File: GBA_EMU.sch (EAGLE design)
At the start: 72 parts, among them J1 USB-MINIB-5PIN, J2 AVR_SPI, Q1 MOSFET-PCHANNEL, SW1 LEFT, SW2 RIGHT, SW3 PWR_SWITCH, U2 FT230X, U4 LM4875, U5 V_REG_LDOSMD2, U7 AZV321, X2 HEADPHONE

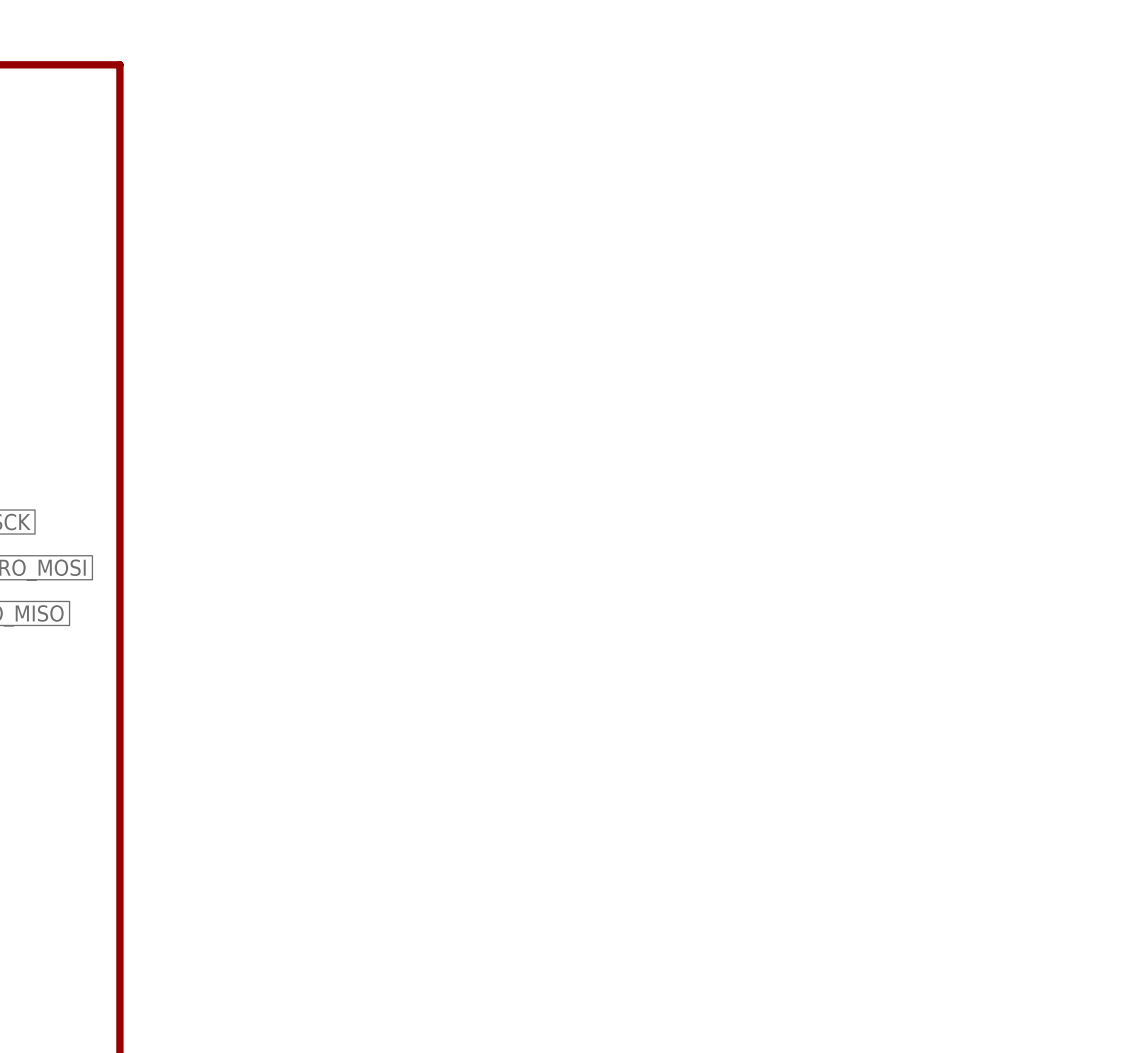
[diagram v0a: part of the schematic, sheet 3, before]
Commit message: added usb hub chip :)
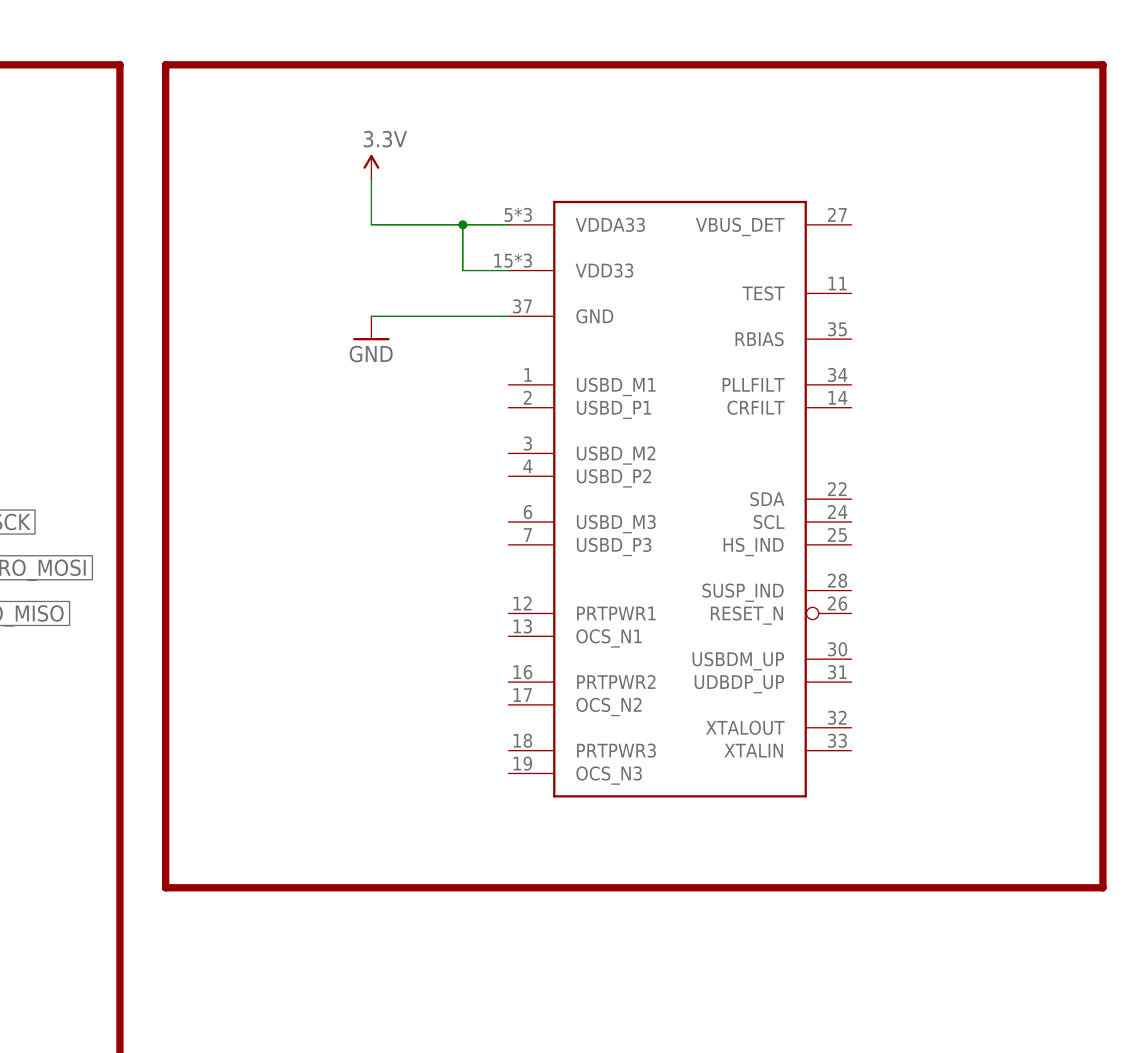
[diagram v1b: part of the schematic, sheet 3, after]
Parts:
- added U$6: USB2523B, custom:USB2523B
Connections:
- net 3.3V: now also U$6.VDD33, U$6.VDDA33
- net GND: now also U$6.GND
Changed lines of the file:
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@@
 <part name="SUPPLY19" library="SparkFun-Aesthetics" deviceset="5V" device=""/>
 <part name="SUPPLY20" library="SparkFun-Aesthetics" deviceset="5V" device=""/>
+<part name="U$6" library="custom" deviceset="USB2523B" device=""/>
+<part name="SUPPLY21" library="SparkFun-Aesthetics" deviceset="3.3V" device=""/>
+<part name="GND34" library="SparkFun-Aesthetics" deviceset="GND" device=""/>
 </parts>
 <sheets>
@@
 <wire x1="7.62" y1="45.72" x2="7.62" y2="167.64" width="0.8128" layer="94"/>
 <text x="10.16" y="170.18" size="1.778" layer="94">Coprocessor</text>
+<wire x1="147.32" y1="167.64" x2="251.46" y2="167.64" width="0.8128" layer="94"/>
+<wire x1="251.46" y1="167.64" x2="251.46" y2="76.2" width="0.8128" layer="94"/>
+<wire x1="251.46" y1="76.2" x2="147.32" y2="76.2" width="0.8128" layer="94"/>
+<wire x1="147.32" y1="76.2" x2="147.32" y2="167.64" width="0.8128" layer="94"/>
 </plain>
 <instances>
@@
 <instance part="SUPPLY19" gate="G$1" x="30.48" y="142.24"/>
 <instance part="SUPPLY20" gate="G$1" x="38.1" y="66.04"/>
+<instance part="U$6" gate="G$1" x="198.12" y="119.38"/>
+<instance part="SUPPLY21" gate="G$1" x="170.18" y="154.94"/>
+<instance part="GND34" gate="1" x="170.18" y="137.16"/>
 </instances>
 <busses>
@@
 <pinref part="GND30" gate="1" pin="GND"/>
 <wire x1="91.44" y1="60.96" x2="91.44" y2="55.88" width="0.1524" layer="91"/>
+</segment>
+<segment>
+<pinref part="U$6" gate="G$1" pin="GND"/>
+<pinref part="GND34" gate="1" pin="GND"/>
+<wire x1="185.42" y1="139.7" x2="170.18" y2="139.7" width="0.1524" layer="91"/>
 </segment>
 </net>
@@
 </segment>
 </net>
+<net name="3.3V" class="0">
+<segment>
+<pinref part="U$6" gate="G$1" pin="VDDA33"/>
+<pinref part="SUPPLY21" gate="G$1" pin="3.3V"/>
+<wire x1="185.42" y1="149.86" x2="180.34" y2="149.86" width="0.1524" layer="91"/>
+<wire x1="180.34" y1="149.86" x2="170.18" y2="149.86" width="0.1524" layer="91"/>
+<wire x1="170.18" y1="149.86" x2="170.18" y2="154.94" width="0.1524" layer="91"/>
+<pinref part="U$6" gate="G$1" pin="VDD33"/>
+<wire x1="185.42" y1="144.78" x2="180.34" y2="144.78" width="0.1524" layer="91"/>
+<wire x1="180.34" y1="144.78" x2="180.34" y2="149.86" width="0.1524" layer="91"/>
+<junction x="180.34" y="149.86"/>
+</segment>
+</net>

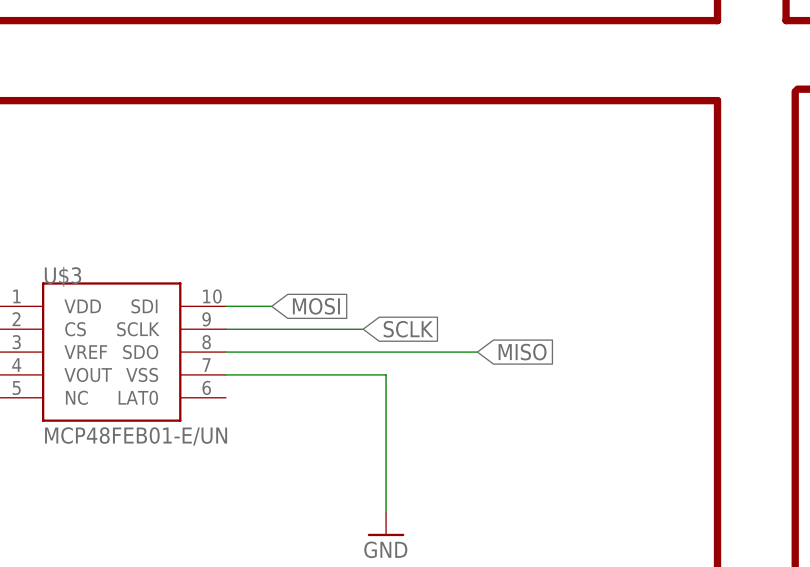
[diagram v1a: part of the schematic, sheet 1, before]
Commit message: connected DAC directly to the Atmega
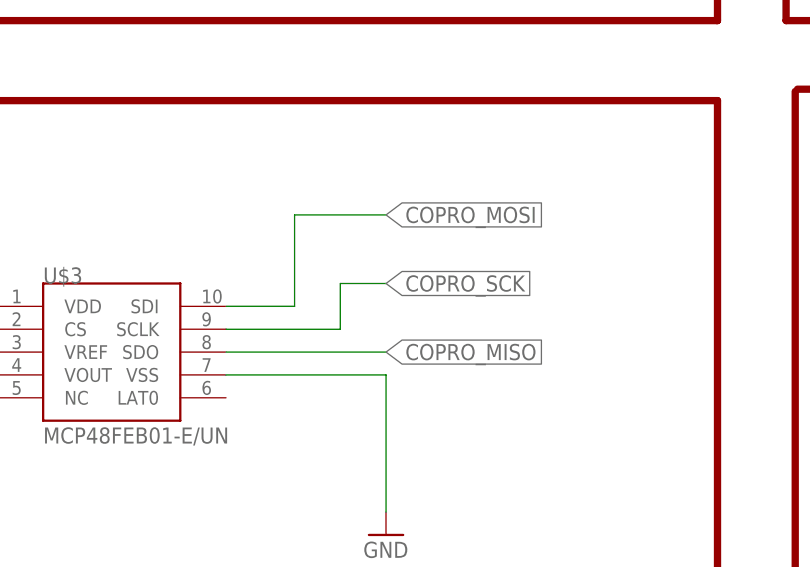
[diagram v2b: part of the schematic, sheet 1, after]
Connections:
- removed net MISO: U$3.SDO
- net COPRO_MISO: now also U$3.SDO
- net COPRO_MOSI: now also U$3.SDI
- net COPRO_SCK: now also U$3.SCLK
- net MOSI: no longer U$3.SDI
- net SCLK: no longer U$3.SCLK
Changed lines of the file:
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@@
 <net name="MOSI" class="0">
-<segment>
-<pinref part="U$3" gate="G$1" pin="SDI"/>
-<wire x1="370.84" y1="104.14" x2="375.92" y2="104.14" width="0.1524" layer="91"/>
-<label x="375.92" y="104.14" size="1.778" layer="95" xref="yes"/>
-</segment>
 <segment>
 <pinref part="TFT1" gate="TFT$1" pin="SDA"/>
@@
 <net name="SCLK" class="0">
 <segment>
-<pinref part="U$3" gate="G$1" pin="SCLK"/>
-<wire x1="370.84" y1="101.6" x2="386.08" y2="101.6" width="0.1524" layer="91"/>
-<label x="386.08" y="101.6" size="1.778" layer="95" xref="yes"/>
-</segment>
-<segment>
 <pinref part="TFT1" gate="TFT$1" pin="SCL"/>
 <wire x1="486.41" y1="88.9" x2="482.6" y2="88.9" width="0.1524" layer="91"/>
@@
 </segment>
 </net>
-<net name="MISO" class="0">
+<net name="COPRO_MISO" class="0">
 <segment>
 <pinref part="U$3" gate="G$1" pin="SDO"/>
-<wire x1="370.84" y1="99.06" x2="398.78" y2="99.06" width="0.1524" layer="91"/>
-<label x="398.78" y="99.06" size="1.778" layer="95" xref="yes"/>
+<wire x1="370.84" y1="99.06" x2="388.62" y2="99.06" width="0.1524" layer="91"/>
+<label x="388.62" y="99.06" size="1.778" layer="95" xref="yes"/>
 </segment>
 </net>
@@
 </segment>
 </net>
+<net name="COPRO_MOSI" class="0">
+<segment>
+<pinref part="U$3" gate="G$1" pin="SDI"/>
+<wire x1="370.84" y1="104.14" x2="378.46" y2="104.14" width="0.1524" layer="91"/>
+<wire x1="378.46" y1="104.14" x2="378.46" y2="114.3" width="0.1524" layer="91"/>
+<wire x1="378.46" y1="114.3" x2="388.62" y2="114.3" width="0.1524" layer="91"/>
+<label x="388.62" y="114.3" size="1.778" layer="95" xref="yes"/>
+</segment>
+</net>
+<net name="COPRO_SCK" class="0">
+<segment>
+<pinref part="U$3" gate="G$1" pin="SCLK"/>
+<wire x1="370.84" y1="101.6" x2="383.54" y2="101.6" width="0.1524" layer="91"/>
+<wire x1="383.54" y1="101.6" x2="383.54" y2="106.68" width="0.1524" layer="91"/>
+<wire x1="383.54" y1="106.68" x2="388.62" y2="106.68" width="0.1524" layer="91"/>
+<label x="388.62" y="106.68" size="1.778" layer="95" xref="yes"/>
+</segment>
+</net>

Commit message: moved some parts arounf
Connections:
- new net JOY_BTN: U$4.BTN
- net 3.3V: now also U$4.HORZ1, U$4.VERT1
- net DOWN: now also COPRO.PD1(INT1/AIN0)
- net JOY_H: no longer U$4.HORZ1, U$4.VERT1
- net LEFT: now also COPRO.PD2(INT2/AIN1/RXD1)
- net RIGHT: now also COPRO.PD3(INT3/TXD1)
- net UP: now also COPRO.PD0(INT0/OC0B)
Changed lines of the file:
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@@
 <part name="POT1" library="adafruit" deviceset="THUMBPOT" device=""/>
 <part name="U$4" library="custom" deviceset="CTS254_JOYSTICK" device="SM"/>
-<part name="GND15" library="SparkFun-Aesthetics" deviceset="GND" device=""/>
-<part name="SUPPLY1" library="SparkFun-Aesthetics" deviceset="3.3V" device=""/>
 <part name="SW4" library="adafruit" deviceset="SWITCH_PUSHBUTTON" device="EVQ-PE"/>
 <part name="SW5" library="adafruit" deviceset="SWITCH_PUSHBUTTON" device="EVQ-PE"/>
@@
 <part name="SUPPLY21" library="SparkFun-Aesthetics" deviceset="3.3V" device=""/>
 <part name="GND34" library="SparkFun-Aesthetics" deviceset="GND" device=""/>
+<part name="SUPPLY1" library="SparkFun-Aesthetics" deviceset="3.3V" device=""/>
+<part name="SUPPLY22" library="SparkFun-Aesthetics" deviceset="3.3V" device=""/>
+<part name="GND15" library="SparkFun-Aesthetics" deviceset="GND" device=""/>
+<part name="GND35" library="SparkFun-Aesthetics" deviceset="GND" device=""/>
+<part name="GND36" library="SparkFun-Aesthetics" deviceset="GND" device=""/>
 </parts>
 <sheets>
@@
 <instance part="U$1" gate="G$1" x="231.14" y="15.24"/>
 <instance part="POT1" gate="SW" x="378.46" y="142.24"/>
-<instance part="U$4" gate="G$1" x="411.48" y="40.64"/>
-<instance part="GND15" gate="1" x="401.32" y="12.7"/>
-<instance part="SUPPLY1" gate="G$1" x="391.16" y="43.18"/>
+<instance part="U$4" gate="G$1" x="429.26" y="40.64"/>
 <instance part="SW4" gate="G$1" x="414.02" y="-2.54"/>
 <instance part="SW5" gate="G$1" x="414.02" y="-10.16"/>
@@
 <instance part="SW6" gate="G$1" x="429.26" y="7.62"/>
 <instance part="SW7" gate="G$1" x="429.26" y="0"/>
+<instance part="SUPPLY1" gate="G$1" x="416.56" y="43.18"/>
+<instance part="SUPPLY22" gate="G$1" x="416.56" y="33.02"/>
+<instance part="GND15" gate="1" x="419.1" y="15.24"/>
+<instance part="GND35" gate="1" x="416.56" y="25.4"/>
+<instance part="GND36" gate="1" x="408.94" y="33.02"/>
 </instances>
 <busses>
@@
 </segment>
 <segment>
-<pinref part="GND15" gate="1" pin="GND"/>
-<wire x1="401.32" y1="15.24" x2="401.32" y2="20.32" width="0.1524" layer="91"/>
-<pinref part="U$4" gate="G$1" pin="BTN2"/>
-<wire x1="401.32" y1="20.32" x2="403.86" y2="20.32" width="0.1524" layer="91"/>
-<pinref part="U$4" gate="G$1" pin="HORZ3"/>
-<wire x1="403.86" y1="27.94" x2="401.32" y2="27.94" width="0.1524" layer="91"/>
-<wire x1="401.32" y1="27.94" x2="401.32" y2="20.32" width="0.1524" layer="91"/>
-<junction x="401.32" y="20.32"/>
-<pinref part="U$4" gate="G$1" pin="VERT3"/>
-<wire x1="403.86" y1="38.1" x2="401.32" y2="38.1" width="0.1524" layer="91"/>
-<wire x1="401.32" y1="38.1" x2="401.32" y2="27.94" width="0.1524" layer="91"/>
-<junction x="401.32" y="27.94"/>
-</segment>
-<segment>
 <pinref part="SW5" gate="G$1" pin="P$2"/>
 <pinref part="GND16" gate="1" pin="GND"/>
@@
 <pinref part="SW6" gate="G$1" pin="P$2"/>
 <pinref part="SW7" gate="G$1" pin="P$2"/>
+</segment>
+<segment>
+<pinref part="GND35" gate="1" pin="GND"/>
+<pinref part="U$4" gate="G$1" pin="HORZ3"/>
+<wire x1="416.56" y1="27.94" x2="421.64" y2="27.94" width="0.1524" layer="91"/>
+</segment>
+<segment>
+<pinref part="GND15" gate="1" pin="GND"/>
+<pinref part="U$4" gate="G$1" pin="BTN2"/>
+<wire x1="419.1" y1="17.78" x2="419.1" y2="20.32" width="0.1524" layer="91"/>
+<wire x1="419.1" y1="20.32" x2="421.64" y2="20.32" width="0.1524" layer="91"/>
+</segment>
+<segment>
+<pinref part="U$4" gate="G$1" pin="VERT3"/>
+<wire x1="421.64" y1="38.1" x2="408.94" y2="38.1" width="0.1524" layer="91"/>
+<wire x1="408.94" y1="38.1" x2="408.94" y2="35.56" width="0.1524" layer="91"/>
+<pinref part="GND36" gate="1" pin="GND"/>
 </segment>
 </net>
@@
 <pinref part="R13" gate="G$1" pin="2"/>
 </segment>
+<segment>
+<pinref part="SUPPLY1" gate="G$1" pin="3.3V"/>
+<pinref part="U$4" gate="G$1" pin="VERT1"/>
+<wire x1="416.56" y1="43.18" x2="421.64" y2="43.18" width="0.1524" layer="91"/>
+</segment>
+<segment>
+<pinref part="U$4" gate="G$1" pin="HORZ1"/>
+<pinref part="SUPPLY22" gate="G$1" pin="3.3V"/>
+<wire x1="421.64" y1="33.02" x2="416.56" y2="33.02" width="0.1524" layer="91"/>
+</segment>
 </net>
 <net name="DAC_REF" class="0">
@@
 <wire x1="325.12" y1="99.06" x2="325.12" y2="88.9" width="0.1524" layer="91"/>
 <label x="325.12" y="88.9" size="1.778" layer="95" rot="R180" xref="yes"/>
-</segment>
-</net>
-<net name="JOY_V" class="0">
-<segment>
-<pinref part="U$4" gate="G$1" pin="VERT2"/>
-<wire x1="403.86" y1="40.64" x2="398.78" y2="40.64" width="0.1524" layer="91"/>
-<label x="401.32" y="40.64" size="1.778" layer="95" rot="R180" xref="yes"/>
-</segment>
-</net>
-<net name="JOY_H" class="0">
-<segment>
-<pinref part="U$4" gate="G$1" pin="VERT1"/>
-<wire x1="403.86" y1="43.18" x2="391.16" y2="43.18" width="0.1524" layer="91"/>
-<pinref part="SUPPLY1" gate="G$1" pin="3.3V"/>
-<pinref part="U$4" gate="G$1" pin="HORZ1"/>
-<wire x1="403.86" y1="33.02" x2="391.16" y2="33.02" width="0.1524" layer="91"/>
-<wire x1="391.16" y1="33.02" x2="391.16" y2="43.18" width="0.1524" layer="91"/>
-<junction x="391.16" y="43.18"/>
-</segment>
-<segment>
-<pinref part="U$4" gate="G$1" pin="HORZ2"/>
-<wire x1="403.86" y1="30.48" x2="398.78" y2="30.48" width="0.1524" layer="91"/>
-<label x="398.78" y="30.48" size="1.778" layer="95" rot="R180" xref="yes"/>
 </segment>
 </net>
@@
 <wire x1="383.54" y1="106.68" x2="388.62" y2="106.68" width="0.1524" layer="91"/>
 <label x="388.62" y="106.68" size="1.778" layer="95" xref="yes"/>
+</segment>
+</net>
+<net name="JOY_BTN" class="0">
+<segment>
+<pinref part="U$4" gate="G$1" pin="BTN"/>
+<wire x1="421.64" y1="22.86" x2="406.4" y2="22.86" width="0.1524" layer="91"/>
+<label x="406.4" y="22.86" size="1.778" layer="95" rot="R180" xref="yes"/>
+</segment>
+</net>
+<net name="JOY_V" class="0">
+<segment>
+<pinref part="U$4" gate="G$1" pin="VERT2"/>
+<wire x1="421.64" y1="40.64" x2="406.4" y2="40.64" width="0.1524" layer="91"/>
+<label x="406.4" y="40.64" size="1.778" layer="95" rot="R180" xref="yes"/>
+</segment>
+</net>
+<net name="JOY_H" class="0">
+<segment>
+<pinref part="U$4" gate="G$1" pin="HORZ2"/>
+<wire x1="421.64" y1="30.48" x2="406.4" y2="30.48" width="0.1524" layer="91"/>
+<label x="406.4" y="30.48" size="1.778" layer="95" rot="R180" xref="yes"/>
 </segment>
 </net>
@@
 </segment>
 </net>
+<net name="UP" class="0">
+<segment>
+<pinref part="COPRO" gate="G$1" pin="PD0(INT0/OC0B)"/>
+<wire x1="104.14" y1="139.7" x2="111.76" y2="139.7" width="0.1524" layer="91"/>
+<wire x1="111.76" y1="139.7" x2="111.76" y2="157.48" width="0.1524" layer="91"/>
+<wire x1="111.76" y1="157.48" x2="114.3" y2="157.48" width="0.1524" layer="91"/>
+<label x="114.3" y="157.48" size="1.778" layer="95" xref="yes"/>
+</segment>
+</net>
+<net name="DOWN" class="0">
+<segment>
+<pinref part="COPRO" gate="G$1" pin="PD1(INT1/AIN0)"/>
+<wire x1="104.14" y1="137.16" x2="114.3" y2="137.16" width="0.1524" layer="91"/>
+<wire x1="114.3" y1="137.16" x2="114.3" y2="152.4" width="0.1524" layer="91"/>
+<wire x1="114.3" y1="152.4" x2="116.84" y2="152.4" width="0.1524" layer="91"/>
+<label x="116.84" y="152.4" size="1.778" layer="95" xref="yes"/>
+</segment>
+</net>
+<net name="LEFT" class="0">
+<segment>
+<pinref part="COPRO" gate="G$1" pin="PD2(INT2/AIN1/RXD1)"/>
+<wire x1="104.14" y1="134.62" x2="116.84" y2="134.62" width="0.1524" layer="91"/>
+<wire x1="116.84" y1="134.62" x2="116.84" y2="147.32" width="0.1524" layer="91"/>
+<wire x1="116.84" y1="147.32" x2="119.38" y2="147.32" width="0.1524" layer="91"/>
+<label x="119.38" y="147.32" size="1.778" layer="95" xref="yes"/>
+</segment>
+</net>
+<net name="RIGHT" class="0">
+<segment>
+<pinref part="COPRO" gate="G$1" pin="PD3(INT3/TXD1)"/>
+<wire x1="104.14" y1="132.08" x2="119.38" y2="132.08" width="0.1524" layer="91"/>
+<wire x1="119.38" y1="132.08" x2="119.38" y2="142.24" width="0.1524" layer="91"/>
+<wire x1="119.38" y1="142.24" x2="121.92" y2="142.24" width="0.1524" layer="91"/>
+<label x="121.92" y="142.24" size="1.778" layer="95" xref="yes"/>
+</segment>
+</net>
